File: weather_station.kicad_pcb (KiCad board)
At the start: 2 copper layers, 54.4 x 102 mm, 28 parts, among them J1 Conn_01x10_Pin, J2 Conn_01x04, J3 Conn_01x04, J5 USB_C_Receptacle_USB2.0_16P, J6 JTAG_connector, SW1 SW_Push, U1 USBLC6-2SC6, U2 AZ1117CH2-3.3, U4 STM32F103RGTx, X1 831066657

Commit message: Updated PCB
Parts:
- moved J40 25.1 mm to (72.1, 123.1)
- moved R40 23.9 mm to (68.0, 116.4)
- moved R41 23.9 mm to (75.5, 114.5)
- moved U40 23.9 mm to (71.8, 115.1)
- moved R42 23.9 mm to (75.5, 116.5)
- moved R43 23.9 mm to (68.0, 114.5)
- moved R28 22.5 mm to (86.4, 118.5), turned to 180 degrees
- moved R29 18.7 mm to (86.4, 120.5), turned to 0 degrees
- moved SW20 16.3 mm to (86.0, 130.8), turned to -90 degrees
- moved C28 14.8 mm to (86.4, 122.5), turned to 0 degrees
- moved J20 14.1 mm to (105.6, 124.3), turned to 0 degrees
- moved J42 14.1 mm to (107.0, 132.2)
- moved J41 14.1 mm to (95.8, 132.2)
- moved U10 3.35 mm to (69.2, 101.8)
- renumbered J6 to J20, J1 to J30, J5 to J40, J2 to J41, J3 to J42, SW1 to SW20, U2 to U10, U4 to U20, U1 to U40, X1 to X20
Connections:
- U20 pad 20: /Display/display_cs -> unconnected-(U20-PA4-Pad20)
- U20 pad 24: /Display/display_extcomin -> /Display/display_cs
- U20 pad 25: /Display/display_extmode -> /Display/display_extcomin
- U20 pad 26: unconnected-(U4-PB0-Pad26) -> /Display/display_extmode
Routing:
- net +5V: track 11.6 -> 65.0 mm, vias 1 -> 3
- net /Microcontroller/reset: track 1.42 -> 34.9 mm, vias 1 -> 0
- net /Microcontroller/swdio: track 0.07 -> 32.9 mm, vias 0 -> 2
- net /Microcontroller/swclk: track 0.00 -> 29.0 mm, vias 0 -> 2
- net /Microcontroller/swo: track 0.00 -> 27.3 mm
- net /Connectors/usb_dm: track 47.5 -> 23.4 mm
- net /Connectors/usb_dp: track 46.8 -> 22.7 mm
- net Net-(U20-PA15): track 40.4 -> 21.1 mm
- net /Connectors/sensor_2_tx: track 48.9 -> 35.5 mm
- net /Connectors/sensor_1_rx: track 45.3 -> 32.0 mm
- net /Connectors/sensor_1_tx: track 44.7 -> 31.4 mm
- net /Connectors/sensor_2_rx: track 49.5 -> 37.0 mm
- net /Display/display_sclk: track 15.9 -> 27.7 mm
- net /Display/display_mosi: track 15.6 -> 26.8 mm
- net /Display/display_extcomin: track 14.5 -> 25.5 mm
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- added copper zone on B.Cu, net +3.3V
- added copper zone on F.Cu, net +3.3V
- added copper zone on B.Cu, net GND
- added copper zone on F.Cu, net GND
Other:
- board size 54.4 x 102 mm -> 54.4 x 89 mm
- board text added: "C21"
- board text added: "Weather station - Richard I."

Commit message: Updated PCB
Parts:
- moved C24 0.74 mm to (94.9, 87.1)
- moved C20 0.73 mm to (94.9, 89.1)
- moved R40 0.43 mm to (68.0, 116.0)
- moved R42 0.43 mm to (75.5, 116.0)
- moved R43 0.43 mm to (68.0, 114.0)
- moved U40 0.43 mm to (71.8, 114.6)
- moved R41 0.43 mm to (75.5, 114.1)
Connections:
- J30 pad PAD: (no net) -> GND
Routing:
- net +5V: track 65.0 -> 65.8 mm, vias 3 -> 2
- net /Microcontroller/swdio: track 32.9 -> 33.6 mm
- net Net-(R29-Pad2): track 6.57 -> 7.23 mm
- net GND: track 15.9 -> 15.5 mm, vias 57 -> 62
- net +3.3V: track 24.9 -> 24.8 mm, vias 33 -> 34

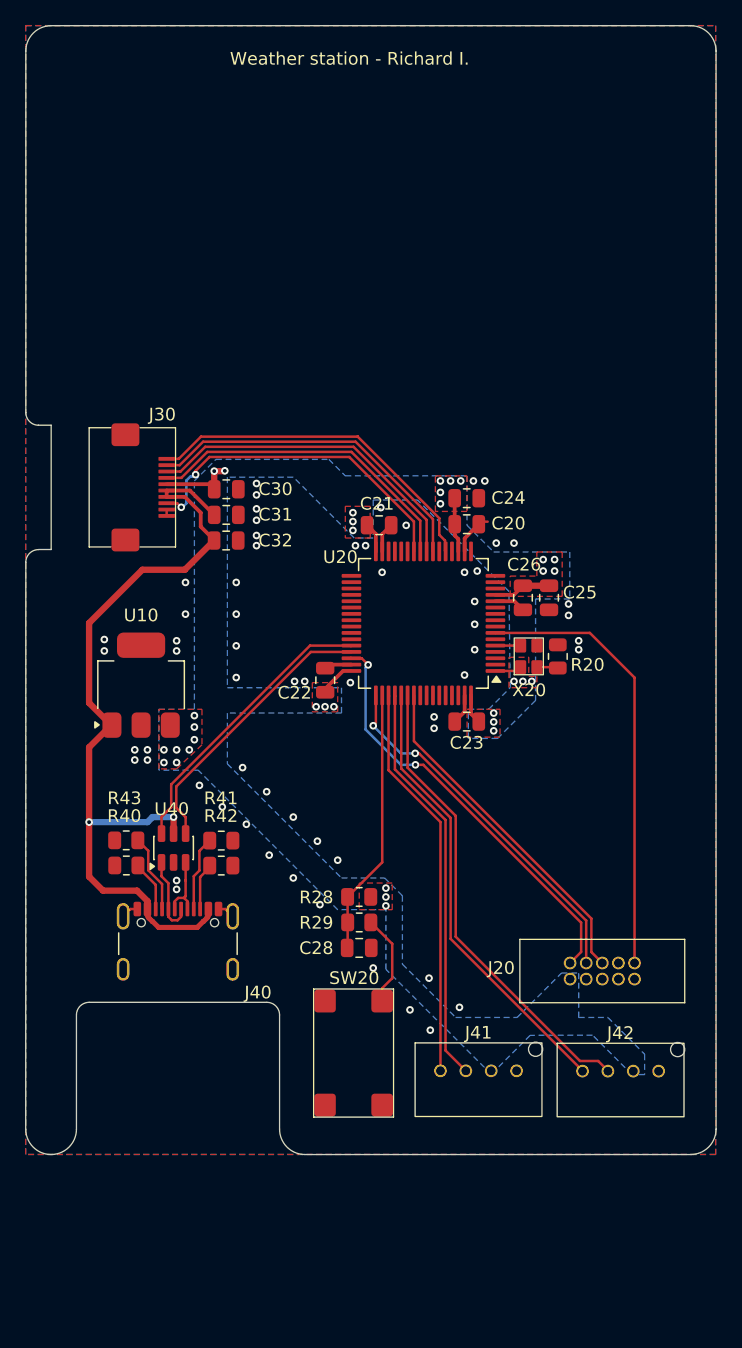
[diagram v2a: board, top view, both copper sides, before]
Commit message: Updated PCB with power planes and vias
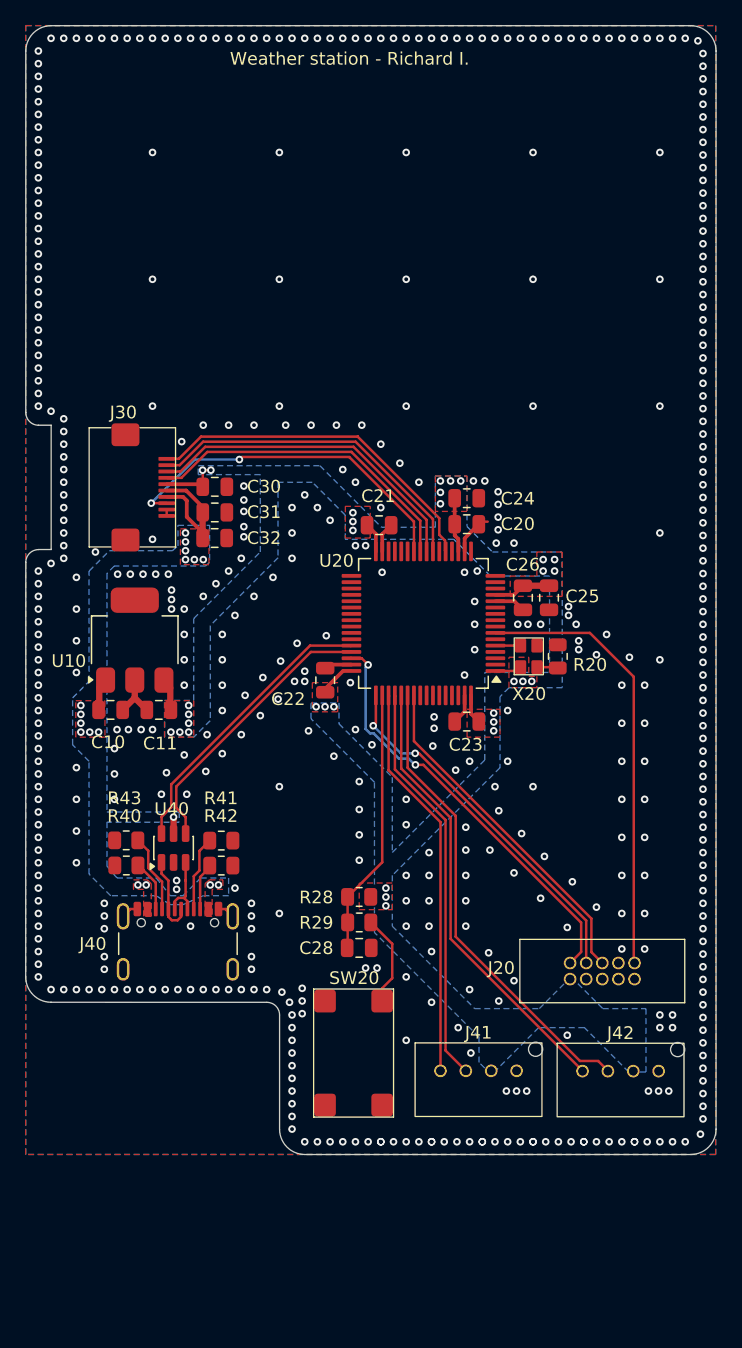
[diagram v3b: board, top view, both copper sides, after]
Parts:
- added C10: 10uF, Capacitor_SMD:C_0805_2012Metric, F.Cu at (66.8, 103.8)
- added C11: 22uF, Capacitor_SMD:C_0805_2012Metric, F.Cu at (70.6, 103.8)
- R29: value 1k -> 0
- moved U10 3.59 mm to (68.7, 98.2)
- moved C30 0.93 mm to (75.0, 86.2)
- moved C31 0.93 mm to (75.0, 88.2)
- moved C32 0.93 mm to (75.0, 90.2)
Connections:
- J30 pad PAD: GND -> (no net)
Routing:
- net +5V: track 65.8 -> 14.9 mm, vias 2 -> 17
- net GND: track 15.5 -> 19.6 mm, vias 62 -> 509
- net +3.3V: track 24.8 -> 26.0 mm, vias 34 -> 32
- net /Display/display_extmode: track 27.0 -> 27.9 mm
- added copper zone on B.Cu, net +5V
- added copper zone on F.Cu, net +5V
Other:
- outline, holes or cut-outs redrawn
